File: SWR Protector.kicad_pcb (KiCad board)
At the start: 2 copper layers, 100 x 100 mm, 29 parts, among them J1 Barrel_Jack, J2 Barrel_Jack, J3 transceiver, J4 antenna, K2 ATX209, Q1 2N3904, T1 1:12, T2 1:12, U1 LM78L05_TO92, U2 LM358

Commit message: changed footprint for BNC, barrel connectors to make them normal
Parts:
- added REF**: MountingHole_4.3mm_M4_DIN965_Pad, MountingHole:MountingHole_4.3mm_M4_DIN965_Pad, F.Cu at (92.1, 79.4)
- added REF**: MountingHole_4.3mm_M4_DIN965_Pad, MountingHole:MountingHole_4.3mm_M4_DIN965_Pad, F.Cu at (177.8, 80.6)
- added REF**: MountingHole_4.3mm_M4_DIN965_Pad, MountingHole:MountingHole_4.3mm_M4_DIN965_Pad, F.Cu at (92.1, 109.9)
- added REF**: MountingHole_4.3mm_M4_DIN965_Pad, MountingHole:MountingHole_4.3mm_M4_DIN965_Pad, F.Cu at (177.8, 109.9)
- J1, J2: footprint Connector_BarrelJack:BarrelJack_CUI_PJ-063AH_Horizontal -> Connector_BarrelJack:BarrelJack_Horizontal
- J3, J4: footprint Connector_Coaxial:BNC_TEConnectivity_1478035_Horizontal -> Connector_Coaxial:BNC_Amphenol_B6252HB-NPP3G-50_Horizontal
- moved J1 3.10 mm to (175.3, 140.3), turned to 180 degrees
- moved J2 2.74 mm to (94.9, 138.4), turned to 0 degrees
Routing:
- net +12V: track 86.8 -> 89.0 mm

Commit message: added mounting holes; checkpoint progress on footprints for connectors
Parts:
- removed REF** (x4): MountingHole_4.3mm_M4_DIN965_Pad, MountingHole:MountingHole_4.3mm_M4_DIN965_Pad
- RV1: footprint Potentiometer_THT:Potentiometer_Alpha_RD901F-40-00D_Single_Vertical -> Potentiometer_THT:Potentiometer_Bourns_3266Y_Vertical
- U2: value LM358 -> DIP8_300
- moved RV1 10.3 mm to (107.3, 141.0), turned to -90 degrees
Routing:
- net +5V: track 117.2 -> 128.4 mm
- net Net-(U2A--): track 19.0 -> 16.5 mm

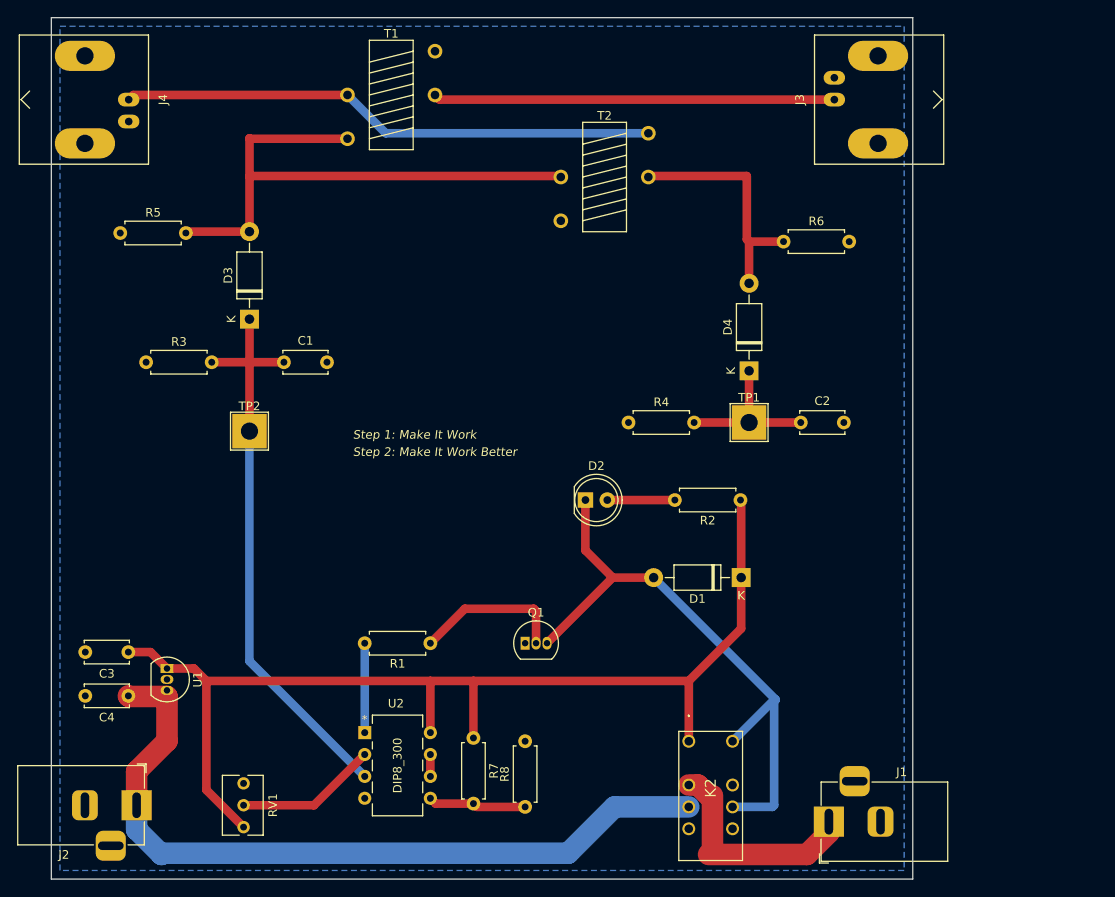
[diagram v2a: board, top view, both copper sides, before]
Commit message: added header for pwr/gnd and both fwd and rev for microcontroler
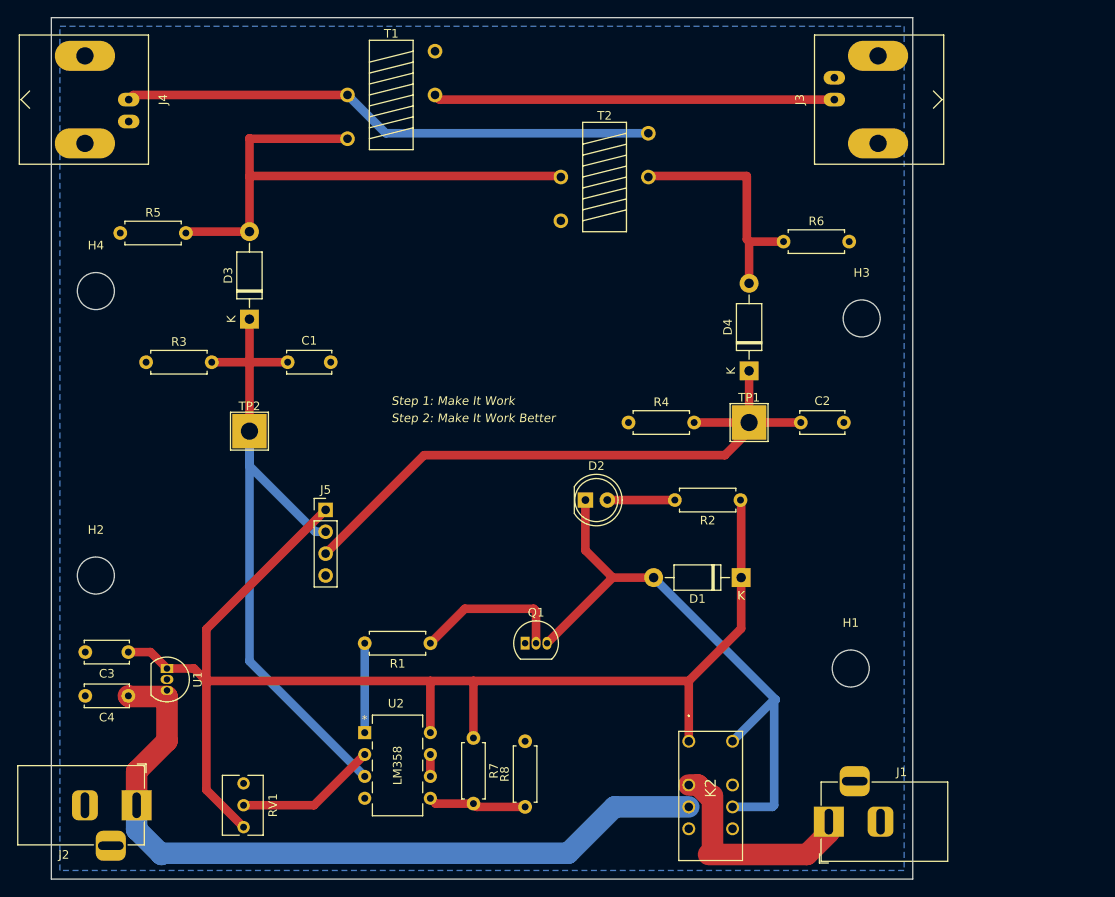
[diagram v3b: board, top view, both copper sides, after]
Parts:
- added H1: MountingHole, MountingHole:MountingHole_4.3mm_M4, F.Cu at (177.8, 122.6)
- added H2: MountingHole, MountingHole:MountingHole_4.3mm_M4, F.Cu at (90.2, 111.8)
- added H3: MountingHole, MountingHole:MountingHole_4.3mm_M4, F.Cu at (179.1, 81.9)
- added H4: MountingHole, MountingHole:MountingHole_4.3mm_M4, F.Cu at (90.2, 78.7)
- added J5: header, Connector_PinHeader_2.54mm:PinHeader_1x04_P2.54mm_Vertical, F.Cu at (116.8, 104.1)
- U2: value DIP8_300 -> LM358
- moved C1 0.44 mm to (112.4, 87.0)
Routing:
- net Net-(D4-K): track 18.4 -> 74.4 mm
- net +5V: track 128.4 -> 154.0 mm
- net Net-(D3-K): track 67.0 -> 83.0 mm

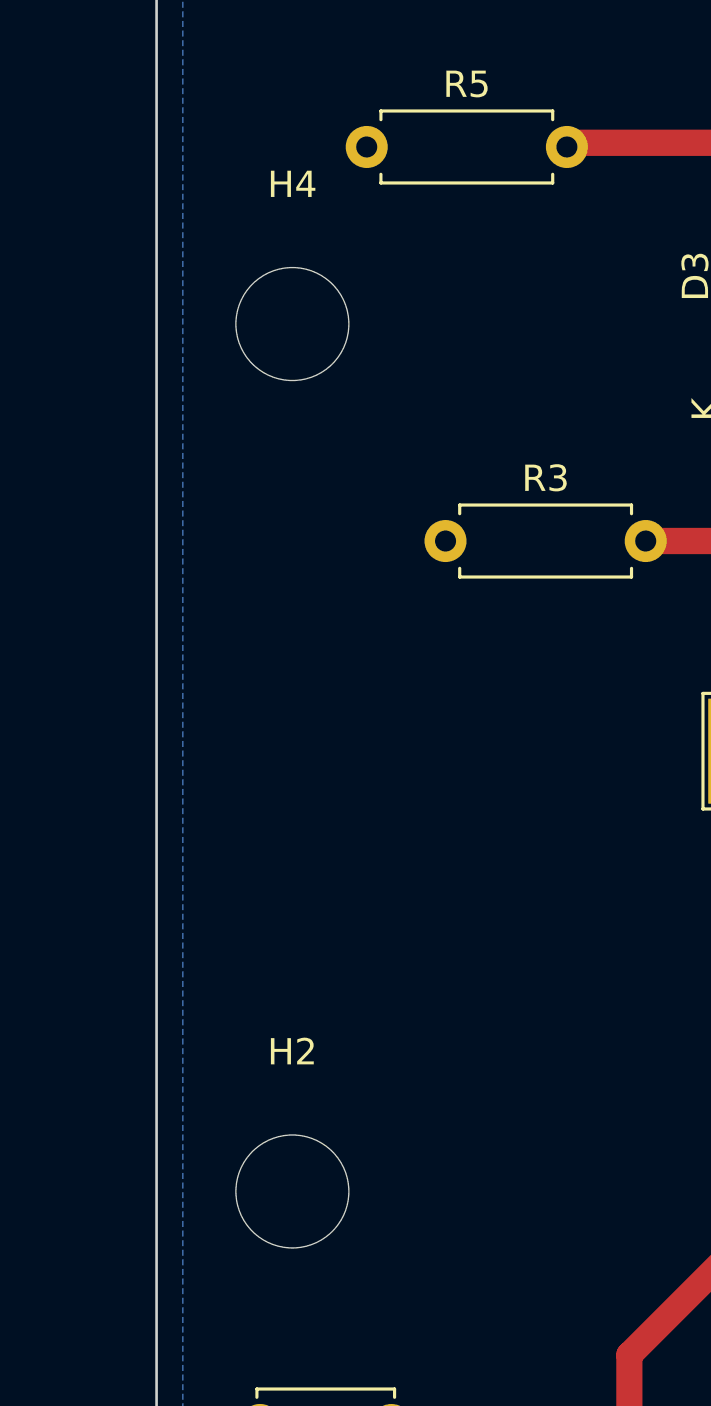
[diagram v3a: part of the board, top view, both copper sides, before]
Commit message: added header pins; fixed some bugs
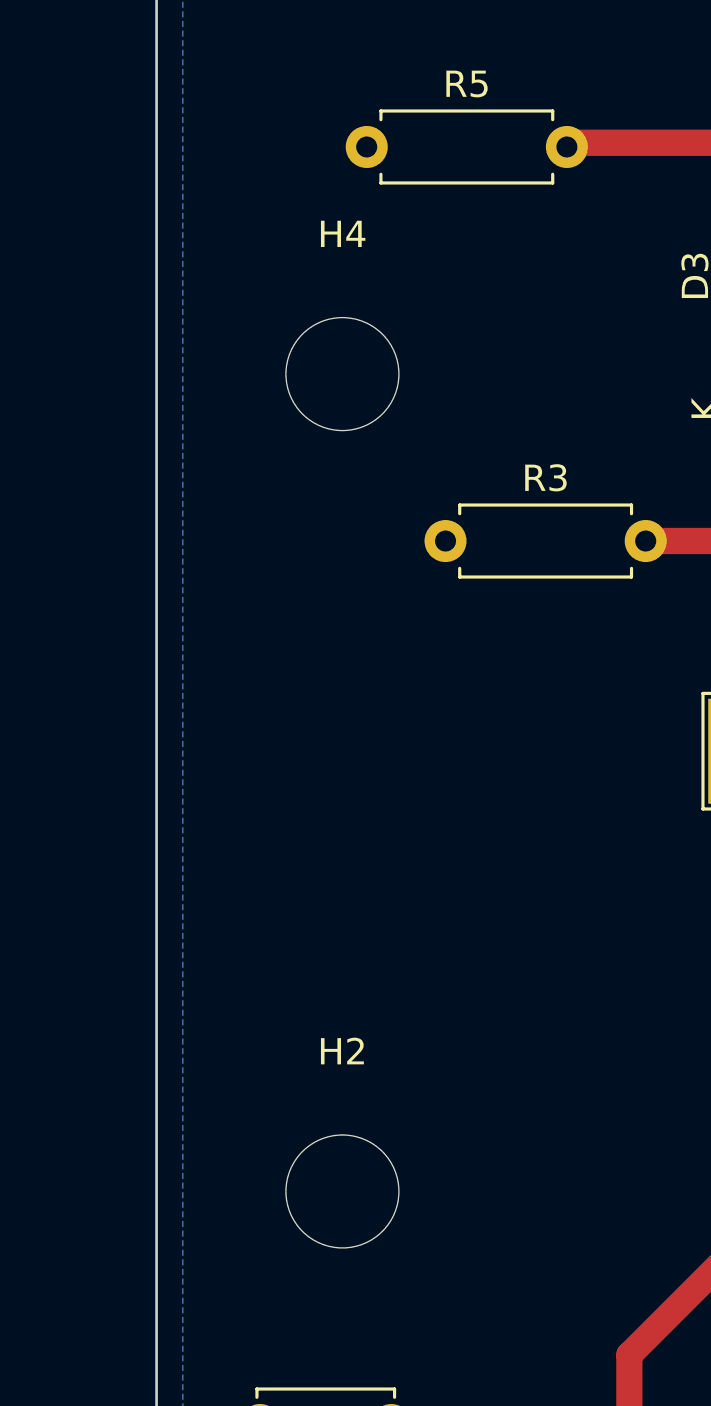
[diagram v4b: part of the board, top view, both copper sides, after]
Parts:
- moved H4 2.69 mm to (92.1, 80.6)
- moved H2 1.91 mm to (92.1, 111.8)
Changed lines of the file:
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@@
   )
   (footprint "MountingHole:MountingHole_4.3mm_M4" (layer "F.Cu")
-    (at 90.17 78.74)
+    (at 92.075 80.645)
     (descr "Mounting Hole 4.3mm, no annular, M4")
     (tags "mounting hole 4.3mm no annular m4")
@@
   )
   (footprint "MountingHole:MountingHole_4.3mm_M4" (layer "F.Cu")
-    (at 90.17 111.76)
+    (at 92.075 111.76)
     (descr "Mounting Hole 4.3mm, no annular, M4")
     (tags "mounting hole 4.3mm no annular m4")

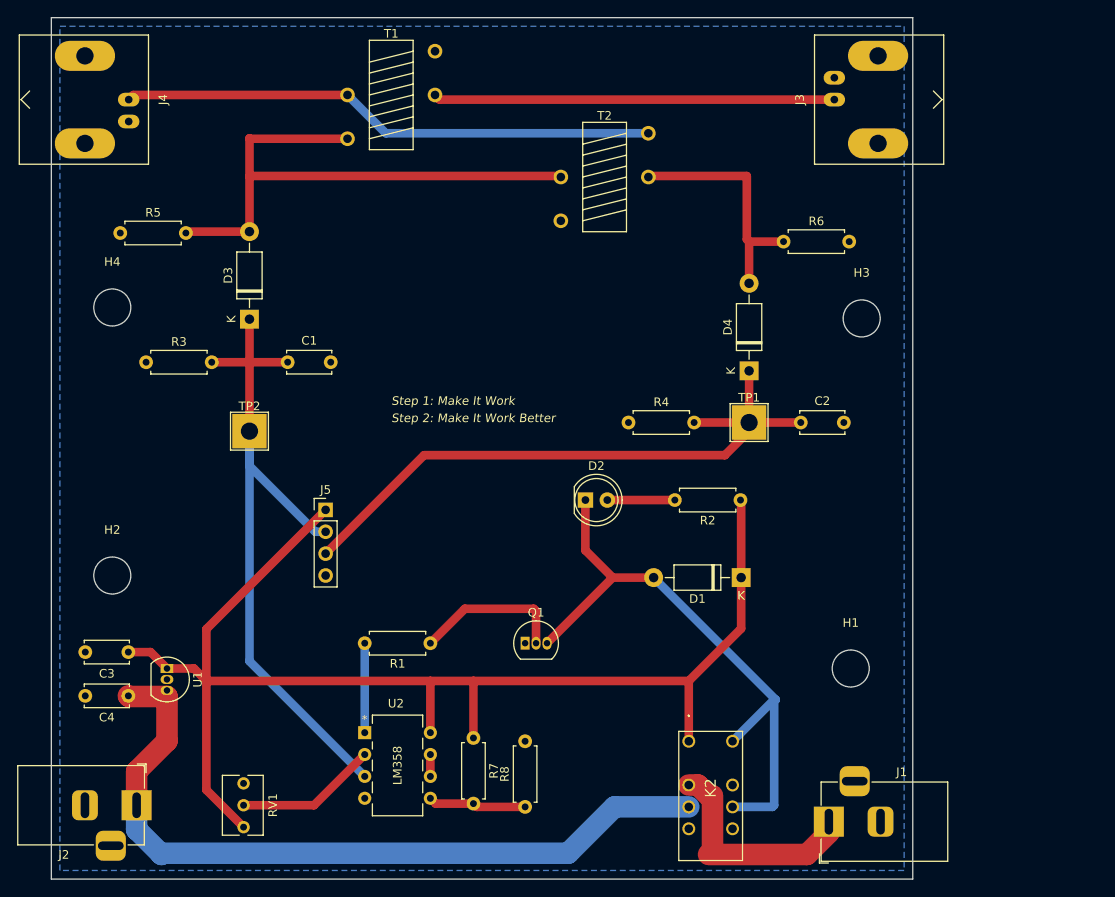
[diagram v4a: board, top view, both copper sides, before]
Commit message: Added ground plane on face layer.  Fixed broken 3D models.
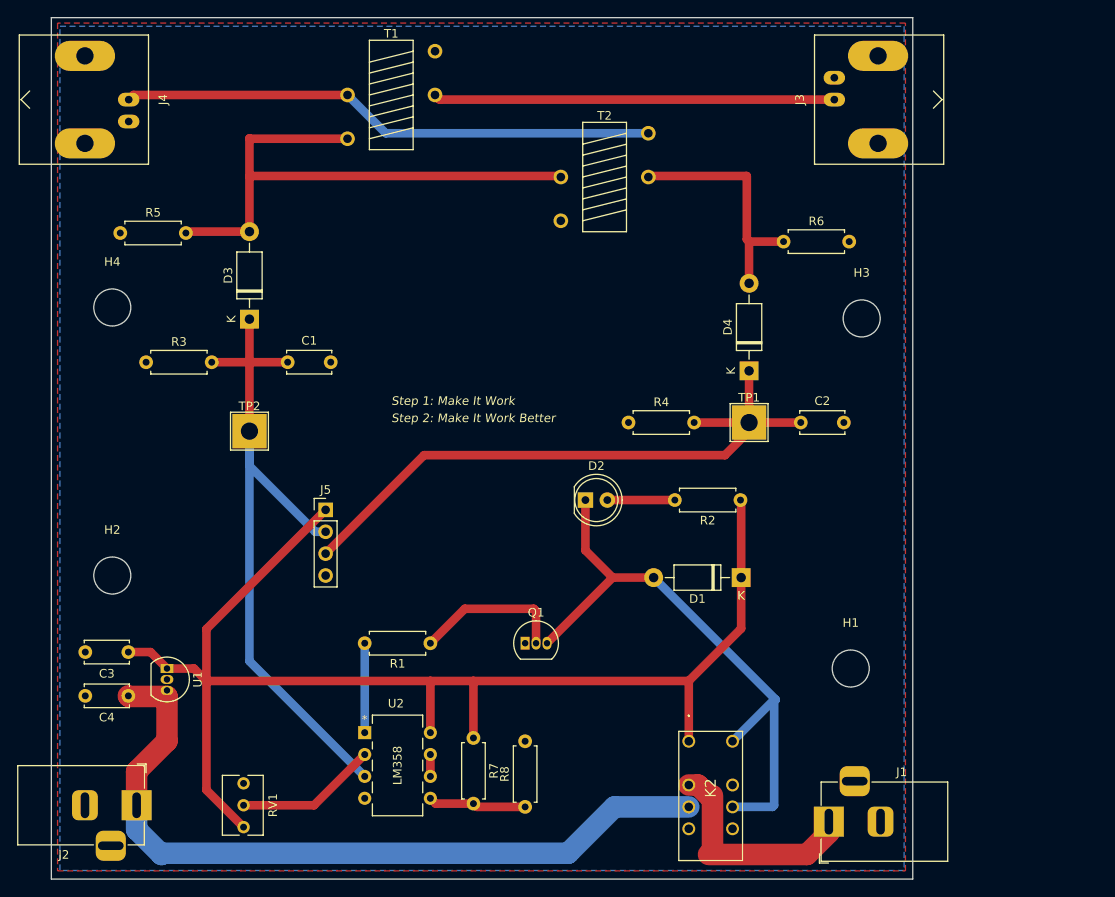
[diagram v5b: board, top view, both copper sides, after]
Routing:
- added copper zone on F.Cu, net GND
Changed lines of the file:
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@@
     (pad "3" thru_hole roundrect (at -3 4.7) (size 3.5 3.5) (drill oval 3 1) (layers "*.Cu" "*.Mask") (roundrect_rratio 0.25)
       (net 2 "GND") (pintype "passive"))
-    (model "${KICAD6_3DMODEL_DIR}/Connector_BarrelJack.3dshapes/BarrelJack_Horizontal.wrl"
-      (offset (xyz 0 0 0))
-      (scale (xyz 1 1 1))
-      (rotate (xyz 0 0 0))
+    (model "${KICAD6_3DMODEL_DIR}/Connector_BarrelJack.3dshapes/BarrelJack_Horizontal.wrl" hide
+      (offset (xyz 0 0 0))
+      (scale (xyz 1 1 1))
+      (rotate (xyz 0 0 0))
+    )
+    (model "${KICAD7_3DMODEL_DIR}/Connector_BarrelJack.3dshapes/BarrelJack_CUI_PJ-063AH_Horizontal.step"
+      (offset (xyz -0.5 0 0))
+      (scale (xyz 1 1 1))
+      (rotate (xyz 0 0 90))
     )
   )
@@
     (pad "8" thru_hole circle (at 0 -7.62) (size 1.524 1.524) (drill 0.8128) (layers "*.Cu" "*.Mask")
       (net 4 "+5V") (pinfunction "V+") (pintype "power_in"))
+    (model "${KIPRJMOD}/models/ON_Semiconductor_-_LM358AN.step"
+      (offset (xyz -3.75 3.75 0))
+      (scale (xyz 1 1 1))
+      (rotate (xyz 0 0 0))
+    )
   )
   (footprint "Resistor_THT:R_Axial_DIN0207_L6.3mm_D2.5mm_P7.62mm_Horizontal" (layer "F.Cu")
@@
     (property "ki_keywords" "BNC SMA SMB SMC LEMO coaxial connector CINCH RCA")
     (attr through_hole)
-    (fp_text reference "J3" (at 0 4 -90) (layer "F.SilkS")
+    (fp_text reference "J3" (at 0 4 90) (layer "F.SilkS")
         (effects (font (size 1 1) (thickness 0.15)))
     )
@@
         (effects (font (size 1 1) (thickness 0.15)))
     )
-    (fp_text user "${REFERENCE}" (at 0 0 -90) (layer "F.Fab")
+    (fp_text user "${REFERENCE}" (at 0 0 90) (layer "F.Fab")
         (effects (font (size 1 1) (thickness 0.15)))
     )
@@
       (rotate (xyz 0 0 0))
     )
+    (model "${KIPRJMOD}/models/connectors_rf/conn_rf.3dshapes/bnc_90_1-1337543-0.wrl"
+      (offset (xyz 0 12.5 0))
+      (scale (xyz 1 1 1))
+      (rotate (xyz 0 0 180))
+    )
   )
   (footprint "MountingHole:MountingHole_4.3mm_M4" (layer "F.Cu")
@@
       (scale (xyz 1 1 1))
       (rotate (xyz 0 0 0))
+    )
+    (model "${KICAD7_3DMODEL_DIR}/Connector_BarrelJack.3dshapes/BarrelJack_CUI_PJ-063AH_Horizontal.step"
+      (offset (xyz -0.5 0 0))
+      (scale (xyz 1 1 1))
+      (rotate (xyz 0 0 90))
     )
   )
@@
       (rotate (xyz 0 0 0))
     )
+    (model "/Volumes/BlueMountain/Users/timborn/Downloads/Relay_Panasonic_TX2-5V/eec.models/Panasonic_-_TX2-5V.step"
+      (offset (xyz 6.5 2.5 0))
+      (scale (xyz 1 1 1))
+      (rotate (xyz 0 0 0))
+    )
   )
   (footprint "MountingHole:MountingHole_4.3mm_M4" (layer "F.Cu")
@@
     (pad "2" thru_hole oval (at 5.08 -5.08 90) (size 3.5 7) (drill 2.01) (layers "*.Cu" "*.Mask")
       (net 2 "GND") (pinfunction "Ext") (pintype "passive"))
-    (model "${KICAD6_3DMODEL_DIR}/Connector_Coaxial.3dshapes/BNC_Amphenol_B6252HB-NPP3G-50_Horizontal.wrl"
-      (offset (xyz 0 0 0))
-      (scale (xyz 1 1 1))
-      (rotate (xyz 0 0 0))
+    (model "/Volumes/BlueMountain/Users/timborn/kikad/kicad-footprints/Connector_Coaxial.pretty/BNC_Amphenol_B6252HB-NPP3G-50_Horizontal.kicad_mod"
+      (offset (xyz 0 0 0))
+      (scale (xyz 1 1 1))
+      (rotate (xyz 0 0 0))
+    )
+    (model "${KIPRJMOD}/models/connectors_rf/conn_rf.3dshapes/bnc_90_1-1337543-0.wrl"
+      (offset (xyz 0 12.5 0))
+      (scale (xyz 1 1 1))
+      (rotate (xyz 0 0 180))
     )
   )
@@
   (segment (start 175.26 140.335) (end 175.26 141.605) (width 2.5) (layer "F.Cu") (net 19))
   (segment (start 175.26 141.605) (end 172.72 144.145) (width 2.5) (layer "F.Cu") (net 19))
+  (zone (net 2) (net_name "GND") (layer "F.Cu") (hatch edge 0.5)
+    (priority 1)
+    (connect_pads (clearance 0.5))
+    (min_thickness 0.25) (filled_areas_thickness no)
+    (fill yes (thermal_gap 0.5) (thermal_bridge_width 0.5))
+    (polygon
+      (pts
+        (xy 85.725 47.625)
+        (xy 85.725 146.05)
+        (xy 184.15 146.05)
+        (xy 184.15 47.625)
+      )
+    )
+  )
   (zone (net 2) (net_name "GND") (layer "B.Cu") (name "GND") (hatch edge 0.5)
     (connect_pads (clearance 0.5))
